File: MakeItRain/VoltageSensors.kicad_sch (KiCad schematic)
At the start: 7 parts, among them IC3 OPA2340PA, J4 Conn_01x01

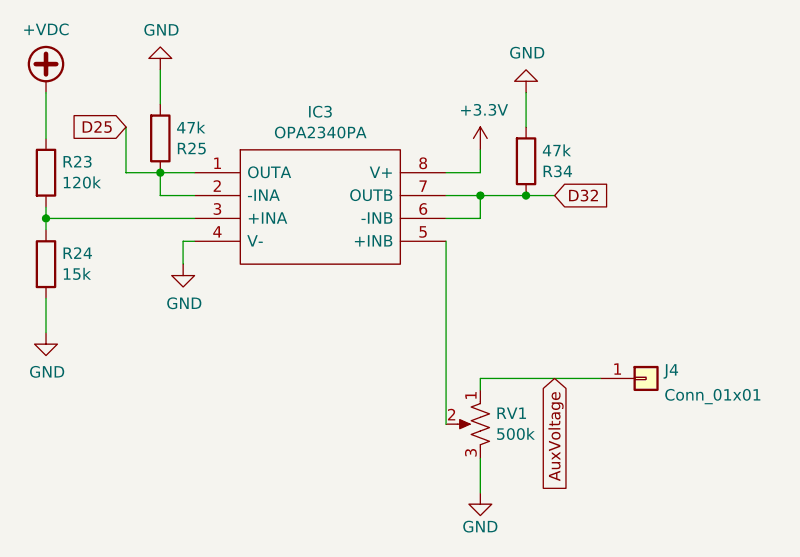
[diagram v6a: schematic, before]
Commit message: Moving into the prototyping testing this deisgn completely phase.
changes
* remapping some pins cause i forgot that ADC2 can not be used while using wifi.
* adding the TH version of the MCP230008 as i don't know the availability of these chips can populate one or the other
* removed zones 5-8 in the code since i hhaven't figured out the daughter board yet. Code not included can be buggy
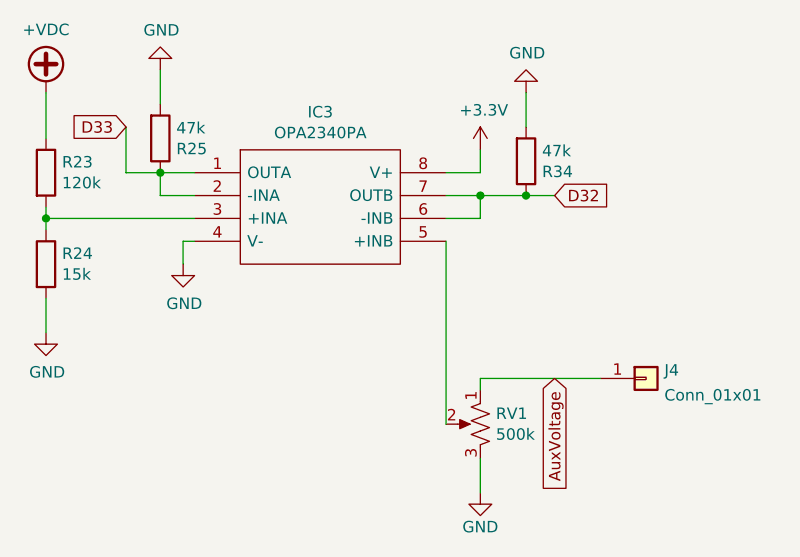
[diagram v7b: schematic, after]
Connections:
- net D25 renamed D33
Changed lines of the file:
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@@
     )
   )
-  (global_label "D25" (shape input) (at 128.27 72.39 180) (fields_autoplaced)
+  (global_label "D33" (shape input) (at 128.27 72.39 180) (fields_autoplaced)
     (effects (font (size 1.27 1.27)) (justify right))
     (property "Intersheet References" "${INTERSHEET_REFS}" (id 0) (at 122.2568 72.3106 0)
